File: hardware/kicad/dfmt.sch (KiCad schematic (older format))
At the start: 36 parts, among them IC1 SI4735-D60, IC2 SI4735-D60, IC3 LE33-SMT, P1 FM ANT, P2 AM ANT, P3 PROG, P4 USB_OTG, Y1 8MHz

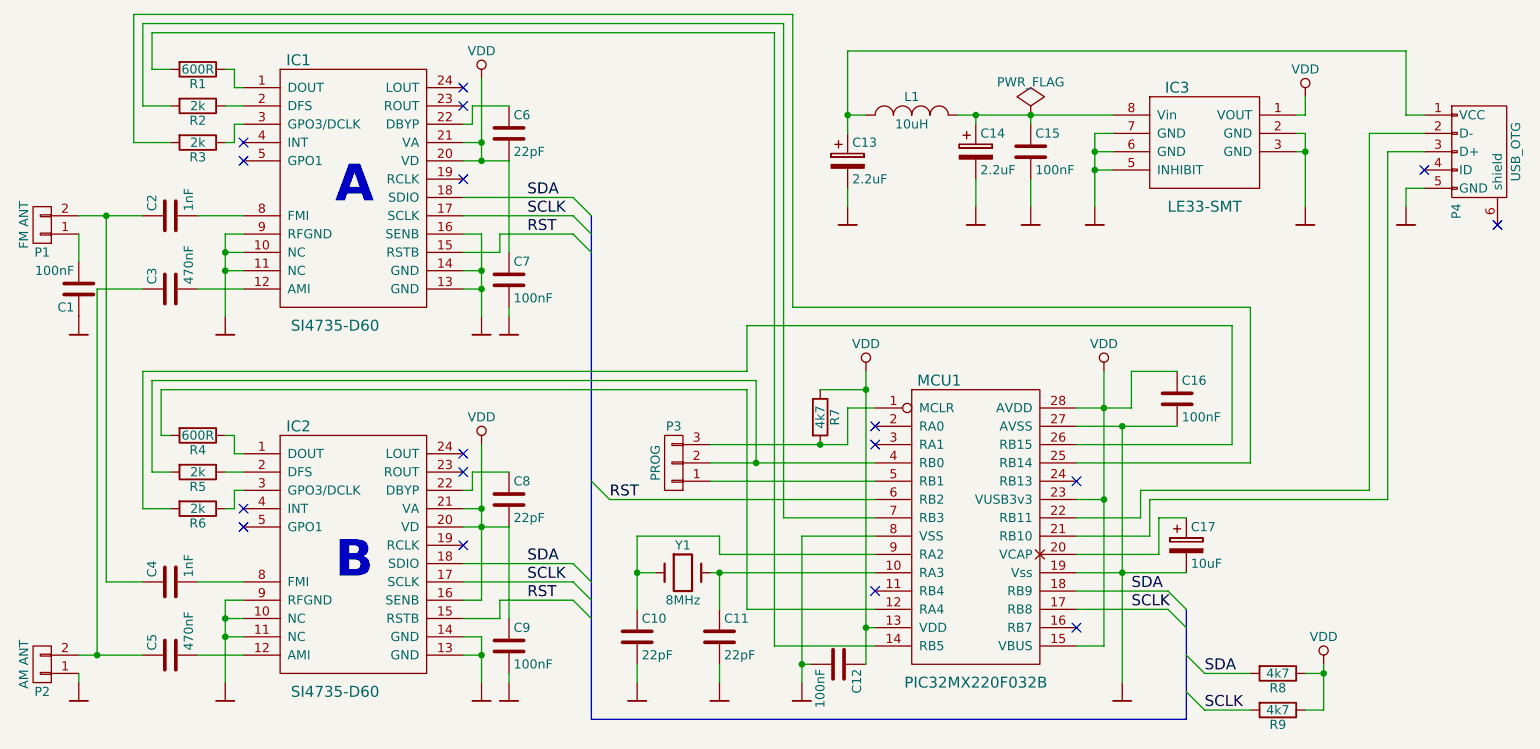
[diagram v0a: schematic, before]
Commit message: finished schematic with DIP mcu and not common DFS and DCLK
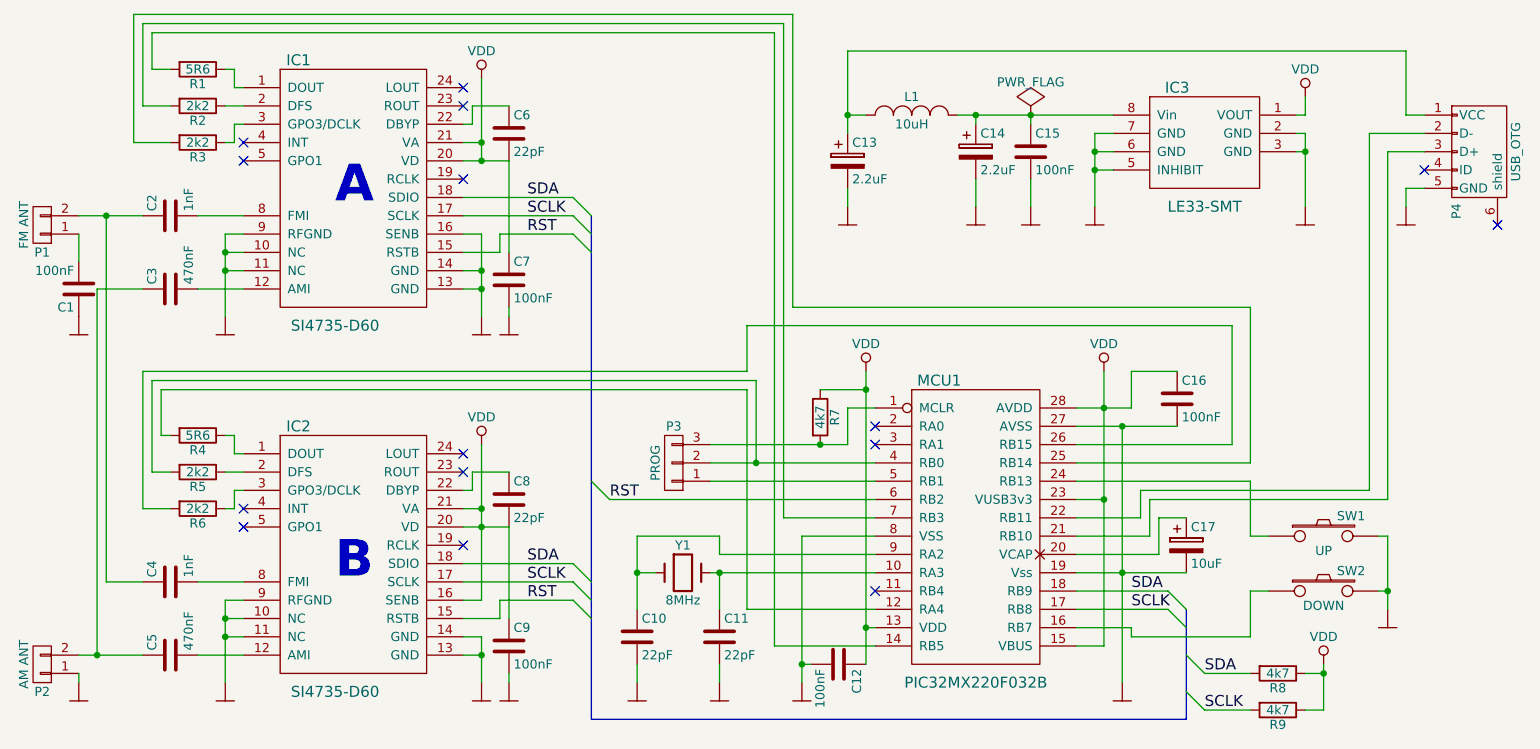
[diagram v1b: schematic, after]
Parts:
- added SW1: UP, dfmt:button-TACT, symbol SW_PUSH
- added SW2: DOWN, dfmt:button-TACT, symbol SW_PUSH
- C1, C10, C11, C12, C15, C16, C2, C3, C4, C5, C6, C7, C8, C9: footprint (none) -> Capacitors_SMD:C_1206_HandSoldering
- C13, C14, C17: footprint (none) -> Capacitors_Tantalum_SMD:TantalC_SizeB_EIA-3528_HandSoldering
- IC1, IC2: footprint (none) -> Housings_SSOP:SSOP-24_3.9x8.7mm_Pitch0.635mm
- IC3: footprint (none) -> Power_Integrations:SO-8
- L1: footprint (none) -> Resistors_SMD:R_1210_HandSoldering
- MCU1: footprint (none) -> Housings_DIP:DIP-28_W7.62mm
- P1, P2: footprint (none) -> Pin_Headers:Pin_Header_Straight_1x02
- P3: footprint (none) -> Pin_Headers:Pin_Header_Straight_1x03
- P4: footprint (none) -> Connect:USB_Mini-B
- R1, R4: value 600R -> 5R6; footprint (none) -> Resistors_SMD:R_1206_HandSoldering
- R2, R3, R5, R6: value 2k -> 2k2; footprint (none) -> Resistors_SMD:R_1206_HandSoldering
- R7, R8, R9: footprint (none) -> Resistors_SMD:R_1206_HandSoldering
- Y1: footprint (none) -> Crystals:Crystal_HC49-SD_SMD
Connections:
- net at MCU1.16 (RB7): now also SW2.1
- net GND: now reaches C16.2, C17.2, MCU1.19 (Vss), MCU1.27 (AVSS)
- net GND: now also C1.1, C10.2, C11.2, C12.2, C13.2, C14.2, C15.2, C7.2, C9.2, IC1.10 (NC), IC1.11 (NC), IC1.13 (GND), IC1.14 (GND), IC1.16 (SENB), IC1.9 (RFGND), IC2.10 (NC), IC2.11 (NC), IC2.13 (GND), IC2.14 (GND), IC2.9 (RFGND), IC3.2 (GND), IC3.3 (GND), IC3.5 (INHIBIT), IC3.6 (GND), IC3.7 (GND), MCU1.8 (VSS), P2.1 (P1), P4.5 (GND), SW1.2, SW2.2
- net at MCU1.24 (RB13): now also SW1.1
- no-connect marks 17 -> 15

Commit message: PCB second try. Unfinished
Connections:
- net GND: now also P4.6 (shield)
- net DOUT_B: now reaches MCU1.12 (RA4), R4.2
- net DOUT_A: now reaches MCU1.14 (RB5), R1.2
- net DCLK: now reaches MCU1.25 (RB14), R3.2
- net DCLK: now also MCU1.26 (RB15), R6.2
- net DFS: now reaches MCU1.4 (RB0), P3.2 (P2), R5.2
- net DFS: now also MCU1.7 (RB3), R2.2
- no-connect marks 15 -> 14
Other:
- moved on the sheet: C12, C13, C14, C15, C2, C3, IC3, L1, P4

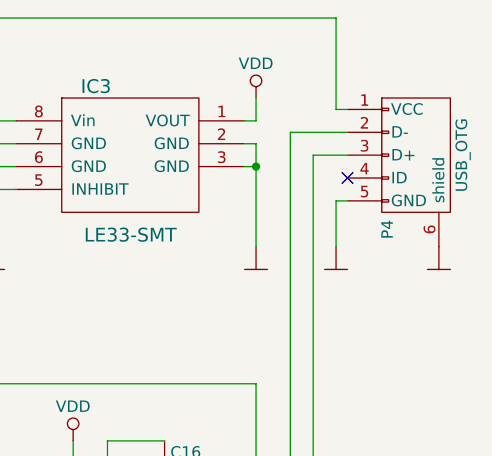
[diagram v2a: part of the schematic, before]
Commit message: MiniB connector changed to mature B, but is not in the middle of board. Still no logo, no holes.
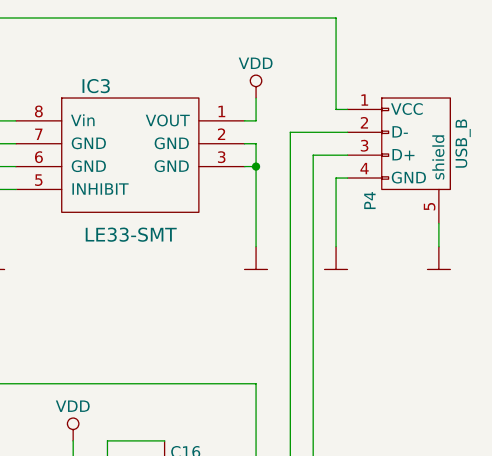
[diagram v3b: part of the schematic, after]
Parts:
- removed P4: USB_OTG, Connect:USB_Mini-B, symbol USB_OTG
- added P4: USB_B, dfmt:USB20_B_F_molex_tht_kink, symbol USB_B
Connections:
- net GND: now also P4.4 (GND), P4.5 (shield)
- net at MCU1.21 (RB10): now also P4.3 (D+)
- net at MCU1.22 (RB11): now also P4.2 (D-)
- net at C13.1, L1.1: now also P4.1 (VCC)
- no-connect marks 14 -> 13
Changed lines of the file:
@@
 LIBS:memory
 LIBS:xilinx
-LIBS:special
 LIBS:microcontrollers
 LIBS:dsp
@@
 	1    7000 4350
 	1    0    0    -1
-$EndComp
-$Comp
-L USB_OTG P4
-U 1 1 55675507
-P 9200 2250
-F 0 "P4" H 9525 2125 50  0000 C CNN
-F 1 "USB_OTG" H 9200 2450 50  0000 C CNN
-F 2 "Connect:USB_Mini-B" V 9150 2150 60  0001 C CNN
-F 3 "" V 9150 2150 60  0000 C CNN
-	1    9200 2250
-	0    1    1    0
 $EndComp
 $Comp
@@
 	8850 1650 8850 2050
 Wire Wire Line
-	8850 2050 8900 2050
-Wire Wire Line
 	5150 4400 5150 4800
 Wire Wire Line
@@
 	7850 3500 8100 3500
 Wire Wire Line
-	8900 2150 8650 2150
-Wire Wire Line
 	8650 2150 8650 4150
 Wire Wire Line
@@
 Wire Wire Line
 	8750 4200 8750 2250
-Wire Wire Line
-	8750 2250 8900 2250
 Wire Bus Line
 	8150 4800 8150 5400
@@
 Connection ~ 5950 5100
 Connection ~ 6400 4900
-NoConn ~ 8900 2350
 NoConn ~ 6450 3800
 NoConn ~ 6450 3900
@@
 $EndComp
 Wire Wire Line
-	8900 2450 8850 2450
-Wire Wire Line
-	8850 2450 8850 2650
+	8850 2350 8850 2650
 $Comp
 L SW_PUSH SW1
@@
 Text Label 6350 4300 2    60   ~ 0
 DFS
+$Comp
+L USB_B P4
+U 1 1 5619540A
+P 9200 2250
+F 0 "P4" H 9400 2050 50  0000 C CNN
+F 1 "USB_B" H 9150 2450 50  0000 C CNN
+F 2 "dfmt:USB20_B_F_molex_tht_kink" V 9150 2150 60  0001 C CNN
+F 3 "" V 9150 2150 60  0000 C CNN
+	1    9200 2250
+	0    1    1    0
+$EndComp
+Wire Wire Line
+	8850 2050 8900 2050
+Wire Wire Line
+	8900 2150 8650 2150
+Wire Wire Line
+	8750 2250 8900 2250
+Wire Wire Line
+	8900 2350 8850 2350
+Wire Wire Line
+	9300 2550 9300 2650
 $EndSCHEMATC

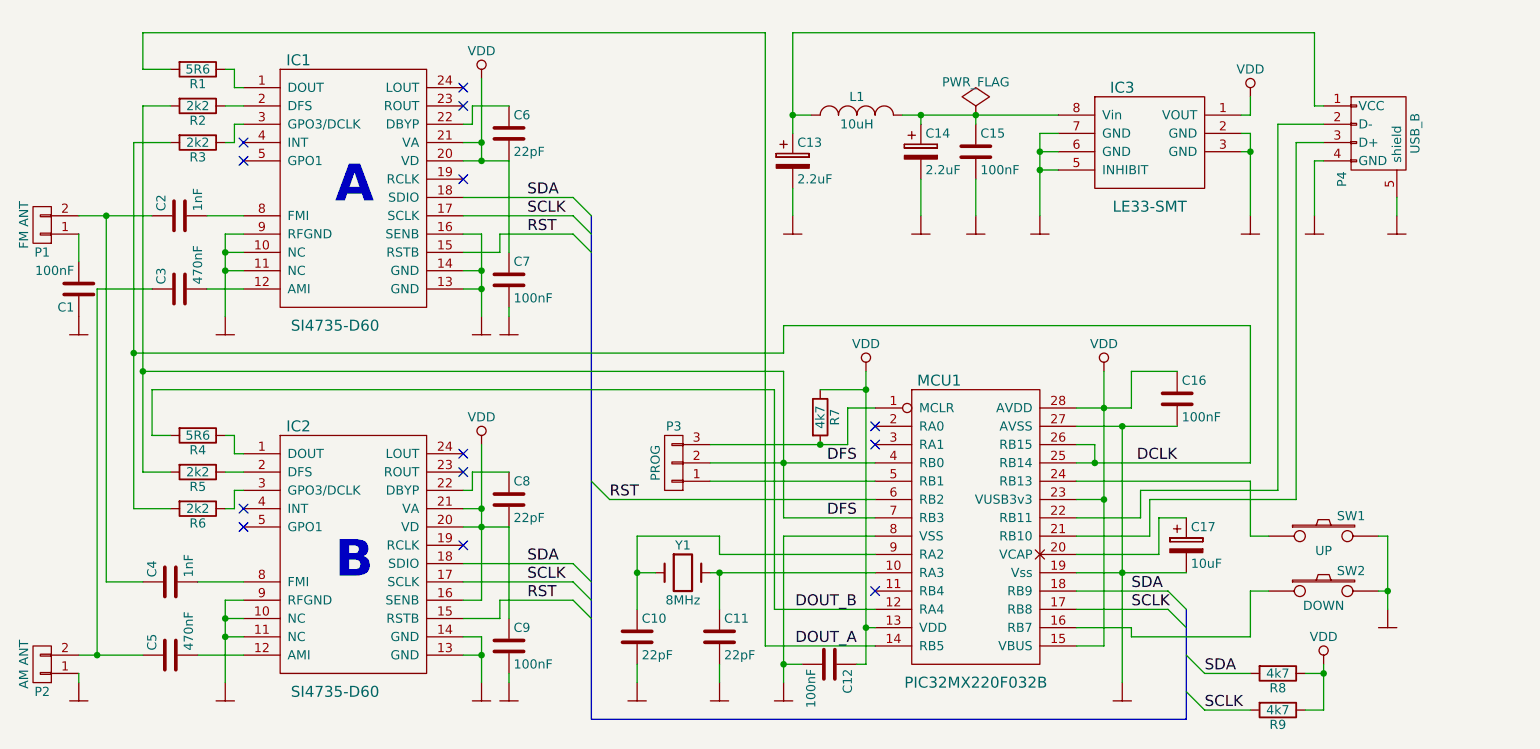
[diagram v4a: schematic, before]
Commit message: Corrected values of some components.
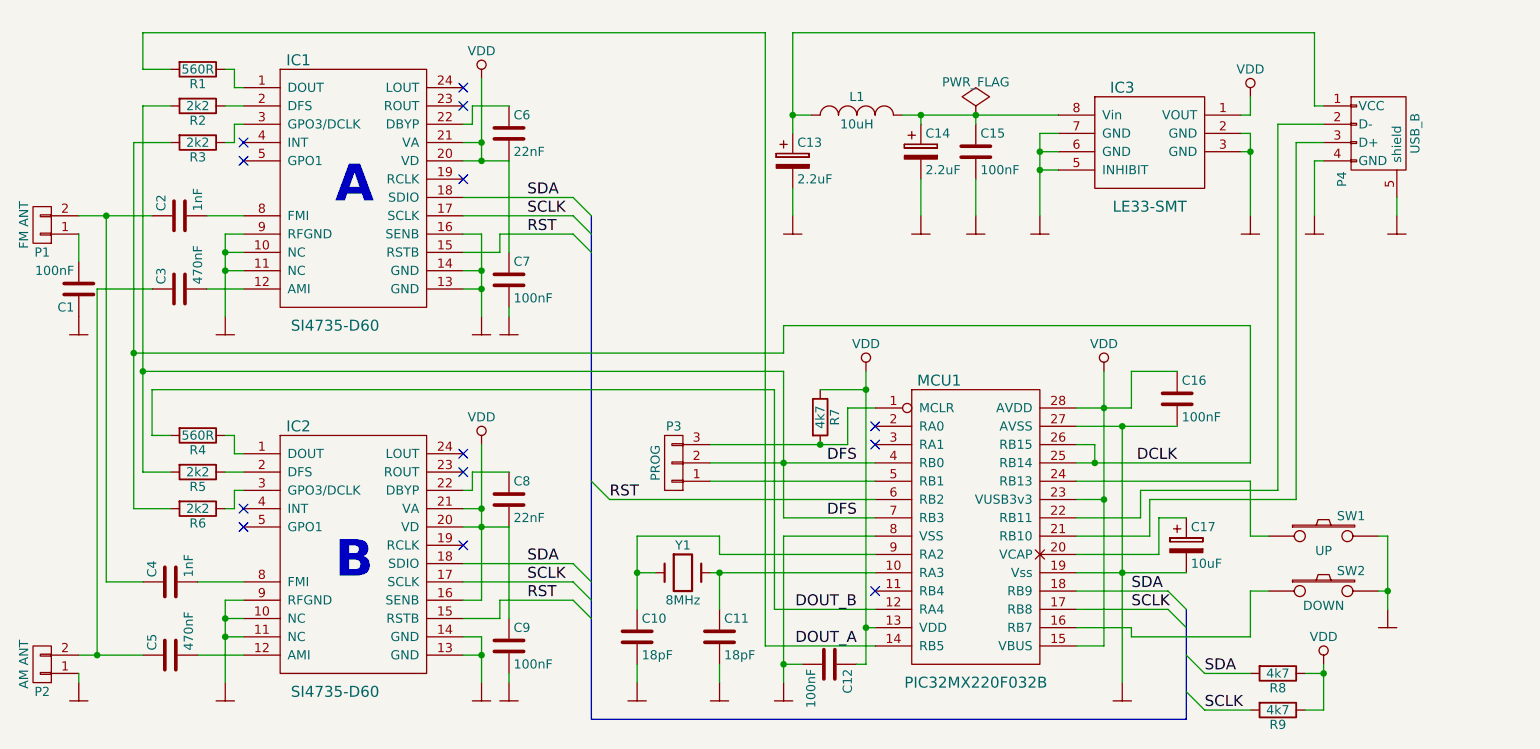
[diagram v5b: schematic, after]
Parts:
- C10, C11: value 22pF -> 18pF
- C6, C8: value 22pF -> 22nF
- R1, R4: value 5R6 -> 560R
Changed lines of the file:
@@
 P 5150 4950
 F 0 "C10" H 5175 5050 50  0000 L CNN
-F 1 "22pF" H 5175 4850 50  0000 L CNN
+F 1 "18pF" H 5175 4850 50  0000 L CNN
 F 2 "Capacitors_SMD:C_1206_HandSoldering" H 5188 4800 30  0001 C CNN
 F 3 "" H 5150 4950 60  0000 C CNN
@@
 P 5600 4950
 F 0 "C11" H 5625 5050 50  0000 L CNN
-F 1 "22pF" H 5625 4850 50  0000 L CNN
+F 1 "18pF" H 5625 4850 50  0000 L CNN
 F 2 "Capacitors_SMD:C_1206_HandSoldering" H 5638 4800 30  0001 C CNN
 F 3 "" H 5600 4950 60  0000 C CNN
@@
 P 2750 3850
 F 0 "R4" V 2830 3850 50  0000 C CNN
-F 1 "5R6" V 2750 3850 50  0000 C CNN
+F 1 "560R" V 2750 3850 50  0000 C CNN
 F 2 "Resistors_SMD:R_1206_HandSoldering" V 2680 3850 30  0001 C CNN
 F 3 "" H 2750 3850 30  0000 C CNN
@@
 P 4450 4200
 F 0 "C8" H 4475 4300 50  0000 L CNN
-F 1 "22pF" H 4475 4100 50  0000 L CNN
+F 1 "22nF" H 4475 4100 50  0000 L CNN
 F 2 "Capacitors_SMD:C_1206_HandSoldering" H 4488 4050 30  0001 C CNN
 F 3 "" H 4450 4200 60  0000 C CNN
@@
 P 2750 1850
 F 0 "R1" V 2830 1850 50  0000 C CNN
-F 1 "5R6" V 2750 1850 50  0000 C CNN
+F 1 "560R" V 2750 1850 50  0000 C CNN
 F 2 "Resistors_SMD:R_1206_HandSoldering" V 2680 1850 30  0001 C CNN
 F 3 "" H 2750 1850 30  0000 C CNN
@@
 P 4450 2200
 F 0 "C6" H 4475 2300 50  0000 L CNN
-F 1 "22pF" H 4475 2100 50  0000 L CNN
+F 1 "22nF" H 4475 2100 50  0000 L CNN
 F 2 "Capacitors_SMD:C_1206_HandSoldering" H 4488 2050 30  0001 C CNN
 F 3 "" H 4450 2200 60  0000 C CNN
